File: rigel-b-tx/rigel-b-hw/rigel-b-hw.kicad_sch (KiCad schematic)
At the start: 48 parts, among them IC1 BALFHB-WL-02D3, J1 Conn_01x03_Pin, J2 436500200, J3 Conn_01x03_Pin, U1 STM32WLE5C8Ux, U2 TPS629206DRLR, U3 CH340X, U4 TYPE-C_16PIN_2MD(073), U5 X1G004131004200, U6 KH-SMA-K513-G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

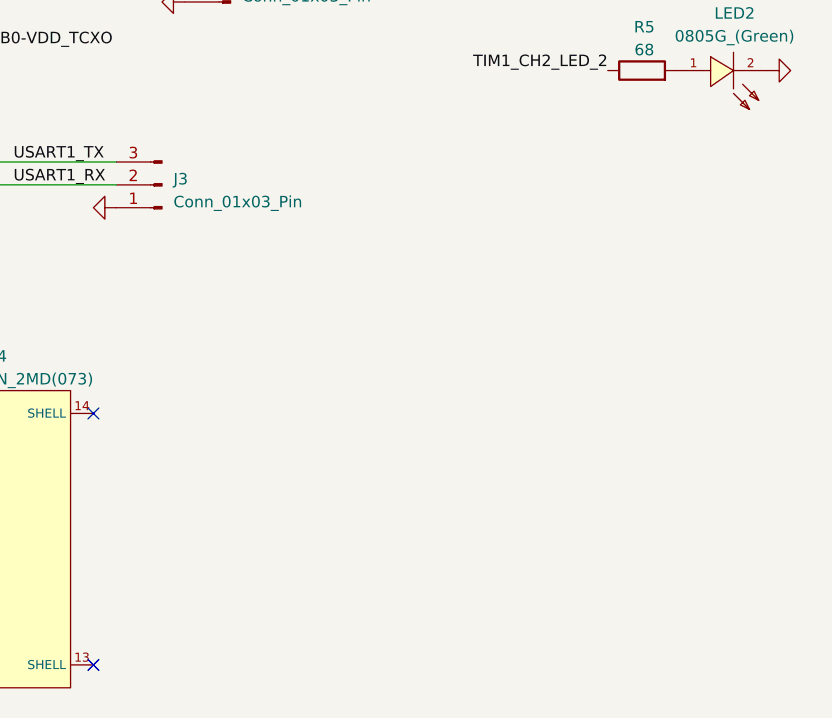
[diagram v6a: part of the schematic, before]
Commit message: gnss schematic+footprint
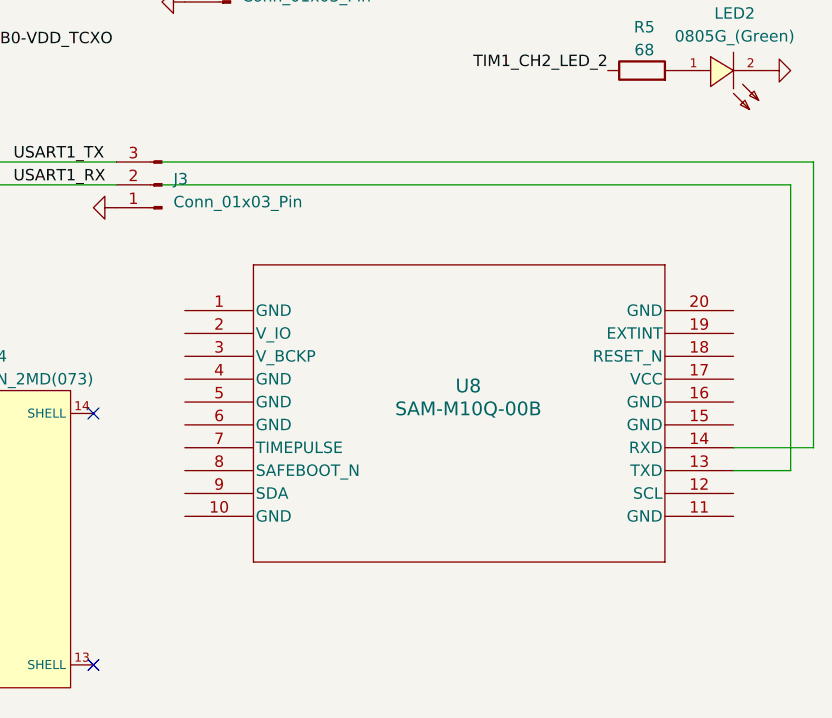
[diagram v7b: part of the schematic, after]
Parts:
- added U8: SAM-M10Q-00B, jlc:SAM-M10Q_UBL, symbol SAM-M10Q-00B:SAM-M10Q-00B
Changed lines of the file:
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@@
+	(wire
+		(pts
+			(xy 190.5 110.49) (xy 260.35 110.49)
+		)
+		(stroke
+			(width 0)
+			(type default)
+		)
+	)
+	(wire
+		(pts
+			(xy 190.5 107.95) (xy 262.89 107.95)
+		)
+		(stroke
+			(width 0)
+			(type default)
+		)
+	)
 	(wire
 		(pts
@@
 	(wire
 		(pts
+			(xy 260.35 110.49) (xy 260.35 142.24)
+		)
+		(stroke
+			(width 0)
+			(type default)
+		)
+	)
+	(wire
+		(pts
 			(xy 115.57 135.89) (xy 119.38 135.89)
 		)
@@
 	(wire
 		(pts
+			(xy 262.89 107.95) (xy 262.89 139.7)
+		)
+		(stroke
+			(width 0)
+			(type default)
+		)
+	)
+	(wire
+		(pts
 			(xy 171.45 59.69) (xy 189.23 59.69)
 		)
@@
 	(wire
 		(pts
+			(xy 254 139.7) (xy 262.89 139.7)
+		)
+		(stroke
+			(width 0)
+			(type default)
+		)
+	)
+	(wire
+		(pts
 			(xy 116.84 45.72) (xy 123.19 45.72)
 		)
@@
 		(pts
 			(xy 140.97 45.72) (xy 140.97 46.99)
+		)
+		(stroke
+			(width 0)
+			(type default)
+		)
+	)
+	(wire
+		(pts
+			(xy 260.35 142.24) (xy 254 142.24)
 		)
 		(stroke
@@
 					(unit 1)
 				)
+			)
+		)
+	)
+	(symbol
+		(lib_id "SAM-M10Q-00B:SAM-M10Q-00B")
+		(at 193.04 124.46 0)
+		(unit 1)
+		(exclude_from_sim no)
+		(in_bom yes)
+		(on_board yes)
+		(dnp no)
+		(property "Reference" "U8"
+			(at 224.536 132.842 0)
+			(effects
+				(font
+					(size 1.524 1.524)
+				)
+			)
+		)
+		(property "Value" "SAM-M10Q-00B"
+			(at 224.536 135.382 0)
+			(effects
+				(font
+					(size 1.524 1.524)
+				)
+			)
+		)
+		(property "Footprint" "jlc:SAM-M10Q_UBL"
+			(at 193.04 124.46 0)
+			(effects
+				(font
+					(size 1.27 1.27)
+					(italic yes)
+				)
+				(hide yes)
+			)
+		)
+		(property "Datasheet" "SAM-M10Q-00B"
+			(at 193.04 124.46 0)
+			(effects
+				(font
+					(size 1.27 1.27)
+					(italic yes)
+				)
+				(hide yes)
+			)
+		)
+		(property "Description" ""
+			(at 193.04 124.46 0)
+			(effects
+				(font
+					(size 1.27 1.27)
+				)
+				(hide yes)
+			)
+		)
+		(pin "9"
+		)
+		(pin "2"
+		)
+		(pin "13"
+		)
+		(pin "11"
+		)
+		(pin "5"
+		)
+		(pin "7"
+		)
+		(pin "8"
+		)
+		(pin "3"
+		)
+		(pin "10"
+		)
+		(pin "1"
+		)
+		(pin "18"
+		)
+		(pin "12"
+		)
+		(pin "14"
+		)
+		(pin "17"
+		)
+		(pin "15"
+		)
+		(pin "16"
+		)
+		(pin "19"
+		)
+		(pin "20"
+		)
+		(pin "4"
+		)
+		(pin "6"
+		)
+		(instances
+			(project ""
+				(path "/5b772f1b-b884-4184-9180-5f1d0867ded9"
+					(reference "U8")
+					(unit 1)
+				)

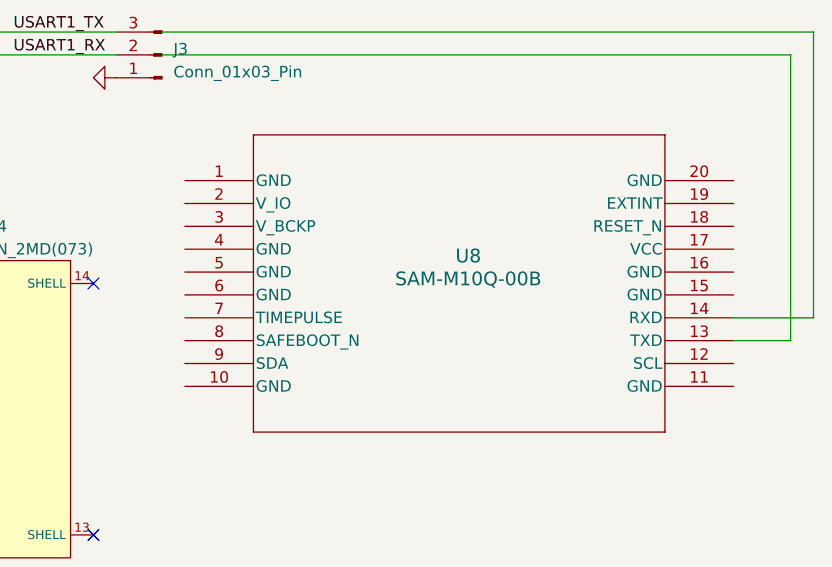
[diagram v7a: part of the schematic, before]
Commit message: added gnd to GPS
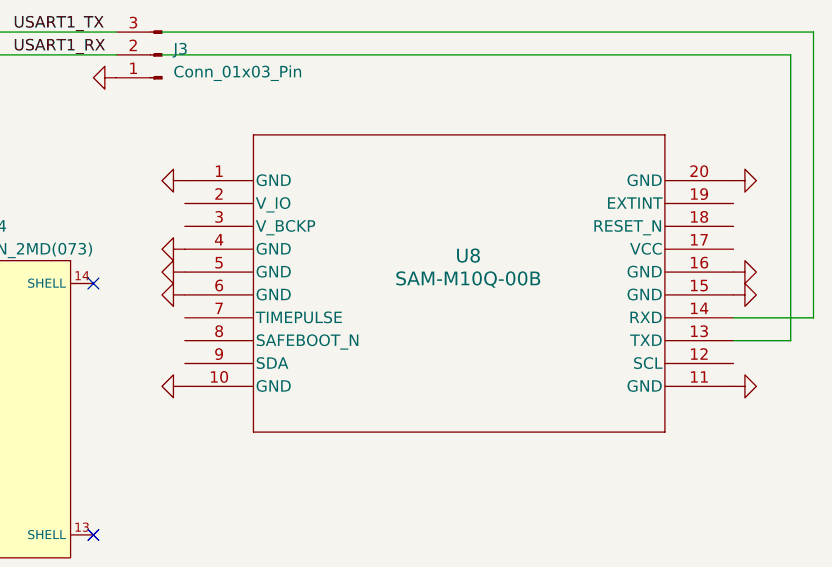
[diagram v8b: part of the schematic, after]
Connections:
- net GND: now also U8.1 (GND), U8.10 (GND), U8.11 (GND), U8.15 (GND), U8.16 (GND), U8.20 (GND), U8.4 (GND), U8.5 (GND), U8.6 (GND)
